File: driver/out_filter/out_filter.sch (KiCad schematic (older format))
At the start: 7 parts, among them J101 X driver, J102 Y driver, J103 Z driver, J104 Source, J105 I sense, J106 V sense

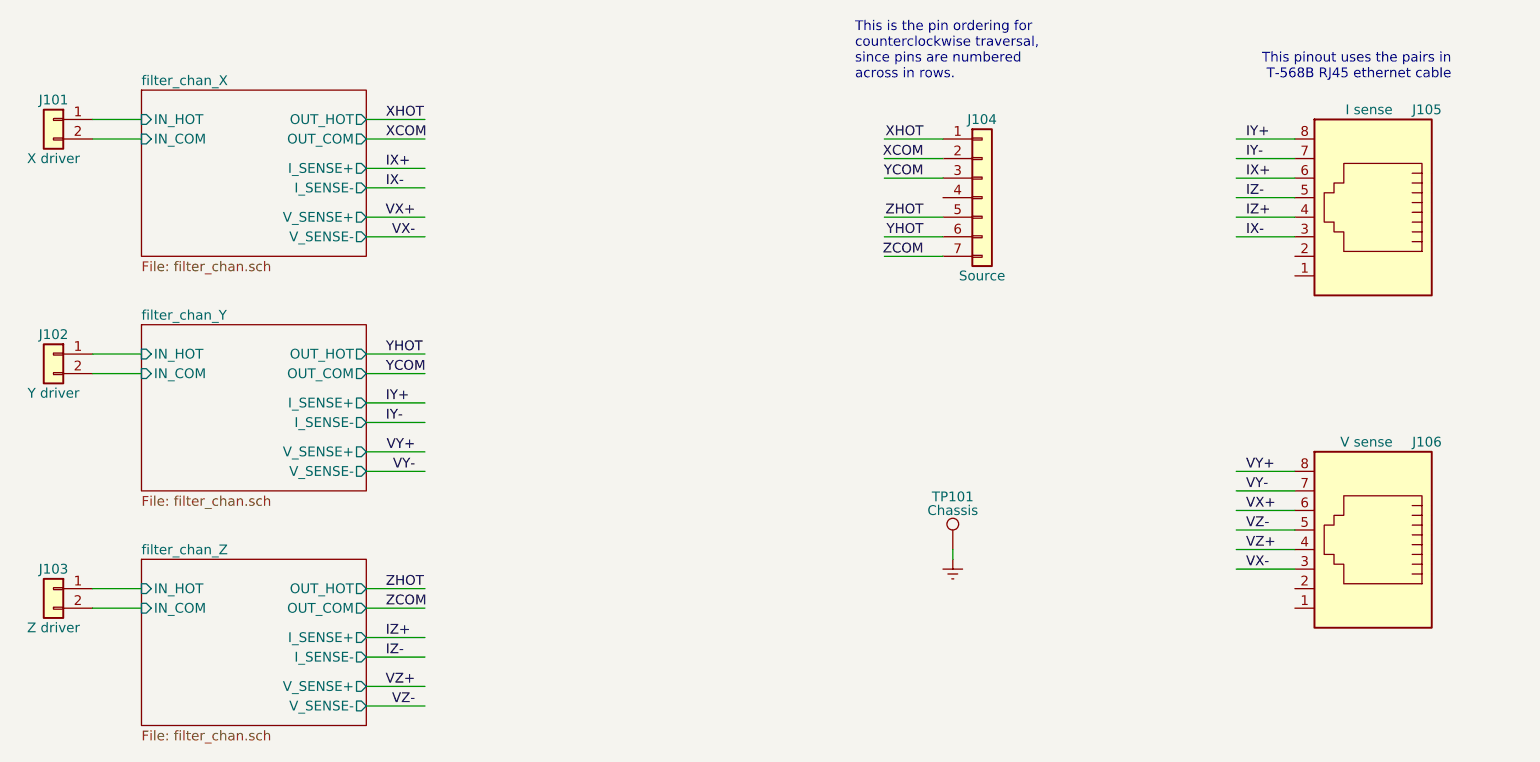
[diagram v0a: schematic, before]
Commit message: Revision 0 of out_filter board.  Tweaks to footprints, reducing pad size.  General routing and pours.
filter_chan.sch:
deleted some testpoints, added input connector.

out_filter.sch:
Added output connector, changed ground testpoint footprint.
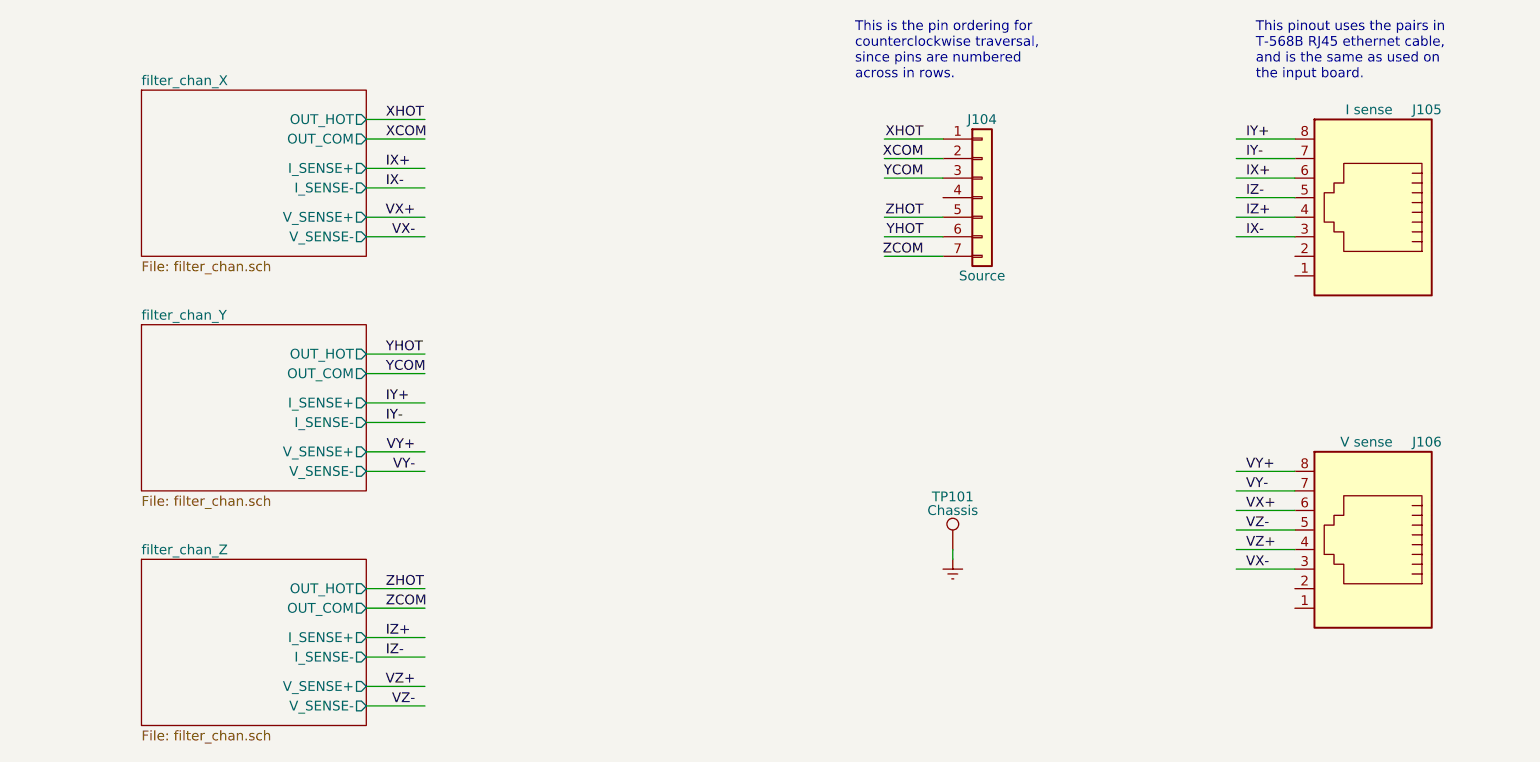
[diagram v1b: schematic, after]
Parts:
- removed J101: X driver, Connector_Molex:Molex_Mini-Fit_Jr_5566-02A_2x01_P4.20mm_Vertical, symbol Connector_Generic:Conn_01x02
- removed J102: Y driver, Connector_Molex:Molex_Mini-Fit_Jr_5566-02A_2x01_P4.20mm_Vertical, symbol Connector_Generic:Conn_01x02
- removed J103: Z driver, Connector_Molex:Molex_Mini-Fit_Jr_5566-02A_2x01_P4.20mm_Vertical, symbol Connector_Generic:Conn_01x02
- J104: Description (none) -> CONN RCPT FMALE 7P SOLDER CUP; Digikey (none) -> H124110-ND; MPN (none) -> JR16RK-7S; Manufacturer (none) -> Hirose Electric Co Ltd
- TP101: footprint TestPoint:TestPoint_Keystone_5000-5004_Miniature -> TestPoint:TestPoint_Keystone_5010-5014_Multipurpose; Description Optional Keystone 5000-5004 -> Optional Keystone 5011
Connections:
- wire segments 43 -> 37
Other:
- note added: "This pinout uses the pairs in \nT-568B RJ45 ethernet cable,\nand is the same as used on \nthe input board."
- note removed: "This pinout uses the pairs in \n T-568B RJ45 ethernet cable"
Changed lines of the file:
@@
 F0 "filter_chan_X" 50
 F1 "filter_chan.sch" 50
-F2 "IN_HOT" I L 3050 2050 50
-F3 "IN_COM" I L 3050 2150 50
-F4 "OUT_HOT" O R 4200 2050 50
-F5 "OUT_COM" O R 4200 2150 50
-F6 "I_SENSE+" O R 4200 2300 50
-F7 "I_SENSE-" O R 4200 2400 50
-F8 "V_SENSE+" O R 4200 2550 50
-F9 "V_SENSE-" O R 4200 2650 50
+F2 "OUT_HOT" O R 4200 2050 50
+F3 "OUT_COM" O R 4200 2150 50
+F4 "I_SENSE+" O R 4200 2300 50
+F5 "I_SENSE-" O R 4200 2400 50
+F6 "V_SENSE+" O R 4200 2550 50
+F7 "V_SENSE-" O R 4200 2650 50
 $EndSheet
 Wire Wire Line
@@
 Text Label 8700 2150 0    50   ~ 0
 IY+
-Text Notes 9750 1850 2    50   ~ 0
-This pinout uses the pairs in \n T-568B RJ45 ethernet cable
+Text Notes 8750 1850 0    50   ~ 0
+This pinout uses the pairs in \nT-568B RJ45 ethernet cable,\nand is the same as used on \nthe input board.
 Wire Wire Line
 	8950 2450 8650 2450
@@
 F0 "filter_chan_Y" 50
 F1 "filter_chan.sch" 50
-F2 "IN_HOT" I L 3050 3250 50
-F3 "IN_COM" I L 3050 3350 50
-F4 "OUT_HOT" O R 4200 3250 50
-F5 "OUT_COM" O R 4200 3350 50
-F6 "I_SENSE+" O R 4200 3500 50
-F7 "I_SENSE-" O R 4200 3600 50
-F8 "V_SENSE+" O R 4200 3750 50
-F9 "V_SENSE-" O R 4200 3850 50
+F2 "OUT_HOT" O R 4200 3250 50
+F3 "OUT_COM" O R 4200 3350 50
+F4 "I_SENSE+" O R 4200 3500 50
+F5 "I_SENSE-" O R 4200 3600 50
+F6 "V_SENSE+" O R 4200 3750 50
+F7 "V_SENSE-" O R 4200 3850 50
 $EndSheet
 $Sheet
@@
 F0 "filter_chan_Z" 50
 F1 "filter_chan.sch" 50
-F2 "IN_HOT" I L 3050 4450 50
-F3 "IN_COM" I L 3050 4550 50
-F4 "OUT_HOT" O R 4200 4450 50
-F5 "OUT_COM" O R 4200 4550 50
-F6 "I_SENSE+" O R 4200 4700 50
-F7 "I_SENSE-" O R 4200 4800 50
-F8 "V_SENSE+" O R 4200 4950 50
-F9 "V_SENSE-" O R 4200 5050 50
+F2 "OUT_HOT" O R 4200 4450 50
+F3 "OUT_COM" O R 4200 4550 50
+F4 "I_SENSE+" O R 4200 4700 50
+F5 "I_SENSE-" O R 4200 4800 50
+F6 "V_SENSE+" O R 4200 4950 50
+F7 "V_SENSE-" O R 4200 5050 50
 $EndSheet
 Wire Wire Line
@@
 Wire Wire Line
 	4200 2300 4500 2300
-$Comp
-L Connector_Generic:Conn_01x02 J101
-U 1 1 5FD8D2E7
-P 2600 2050
-F 0 "J101" H 2600 2150 50  0000 C CNN
-F 1 "X driver" H 2600 1850 50  0000 C CNN
-F 2 "Connector_Molex:Molex_Mini-Fit_Jr_5566-02A_2x01_P4.20mm_Vertical" H 2600 2050 50  0001 C CNN
-F 3 "https://www.molex.com/pdm_docs/ps/PS-5556-001.pdf" H 2600 2050 50  0001 C CNN
-F 4 "CONN HEADER VERT 2POS" H 2600 2050 50  0001 C CNN "Description"
-F 5 "WM23800-ND" H 2600 2050 50  0001 C CNN "Digikey"
-F 6 "0039288020" H 2600 2050 50  0001 C CNN "MPN"
-F 7 "Molex" H 2600 2050 50  0001 C CNN "Manufacturer"
-F 8 "OF.7" H 2600 2050 50  0001 C CNN "DK line"
-	1    2600 2050
-	-1   0    0    -1
-$EndComp
-Wire Wire Line
-	2800 2050 3050 2050
-Wire Wire Line
-	2800 2150 3050 2150
-$Comp
-L Connector_Generic:Conn_01x02 J102
-U 1 1 5FD8F599
-P 2600 3250
-F 0 "J102" H 2600 3350 50  0000 C CNN
-F 1 "Y driver" H 2600 3050 50  0000 C CNN
-F 2 "Connector_Molex:Molex_Mini-Fit_Jr_5566-02A_2x01_P4.20mm_Vertical" H 2600 3250 50  0001 C CNN
-F 3 "https://www.molex.com/pdm_docs/ps/PS-5556-001.pdf" H 2600 3250 50  0001 C CNN
-F 4 "CONN HEADER VERT 2POS" H 2600 3250 50  0001 C CNN "Description"
-F 5 "WM23800-ND" H 2600 3250 50  0001 C CNN "Digikey"
-F 6 "0039288020" H 2600 3250 50  0001 C CNN "MPN"
-F 7 "Molex" H 2600 3250 50  0001 C CNN "Manufacturer"
-F 8 "OF.7" H 2600 3250 50  0001 C CNN "DK line"
-	1    2600 3250
-	-1   0    0    -1
-$EndComp
-Wire Wire Line
-	2800 3250 3050 3250
-Wire Wire Line
-	2800 3350 3050 3350
-$Comp
-L Connector_Generic:Conn_01x02 J103
-U 1 1 5FD8FC32
-P 2600 4450
-F 0 "J103" H 2600 4550 50  0000 C CNN
-F 1 "Z driver" H 2600 4250 50  0000 C CNN
-F 2 "Connector_Molex:Molex_Mini-Fit_Jr_5566-02A_2x01_P4.20mm_Vertical" H 2600 4450 50  0001 C CNN
-F 3 "https://www.molex.com/pdm_docs/ps/PS-5556-001.pdf" H 2600 4450 50  0001 C CNN
-F 4 "CONN HEADER VERT 2POS" H 2600 4450 50  0001 C CNN "Description"
-F 5 "WM23800-ND" H 2600 4450 50  0001 C CNN "Digikey"
-F 6 "0039288020" H 2600 4450 50  0001 C CNN "MPN"
-F 7 "Molex" H 2600 4450 50  0001 C CNN "Manufacturer"
-F 8 "OF.7" H 2600 4450 50  0001 C CNN "DK line"
-	1    2600 4450
-	-1   0    0    -1
-$EndComp
-Wire Wire Line
-	2800 4450 3050 4450
-Wire Wire Line
-	2800 4550 3050 4550
 Wire Wire Line
 	8950 3850 8650 3850
@@
 F 1 "Source" H 7350 2050 50  0000 C CNN
 F 2 "input:HIROSE_JR16RK-7S" H 7350 2450 50  0001 C CNN
-F 3 "~" H 7350 2450 50  0001 C CNN
+F 3 "https://www.hirose.com/product/document?clcode=CL0114-0541-1-00&productname=JR13JK-3S&series=JR&documenttype=Catalog&lang=en&documentid=D49414_en" H 7350 2450 50  0001 C CNN
+F 4 "CONN RCPT FMALE 7P SOLDER CUP" H 7350 2450 50  0001 C CNN "Description"
+F 5 "H124110-ND" H 7350 2450 50  0001 C CNN "Digikey"
+F 6 "JR16RK-7S" H 7350 2450 50  0001 C CNN "MPN"
+F 7 "Hirose Electric Co Ltd" H 7350 2450 50  0001 C CNN "Manufacturer"
 	1    7350 2450
 	1    0    0    -1
@@
 F 0 "TP101" H 7200 4520 50  0000 C CNN
 F 1 "Chassis" H 7200 4450 50  0000 C CNN
-F 2 "TestPoint:TestPoint_Keystone_5000-5004_Miniature" H 7400 4250 50  0001 C CNN
+F 2 "TestPoint:TestPoint_Keystone_5010-5014_Multipurpose" H 7400 4250 50  0001 C CNN
 F 3 "http://keyelco.com/userAssets/file/M65p56.pdf" H 7400 4250 50  0001 C CNN
-F 4 "Optional Keystone 5000-5004" H 7200 4250 50  0001 C CNN "Description"
+F 4 "Optional Keystone 5011" H 7200 4250 50  0001 C CNN "Description"
 F 5 "DNP" H 7200 4250 50  0001 C CNN "MPN"
 F 6 "Keystone Electronics" H 7200 4250 50  0001 C CNN "Manufacturer"
